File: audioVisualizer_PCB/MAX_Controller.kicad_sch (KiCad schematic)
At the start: 16 parts, among them J10 Conn_01x08_Socket, J11 Conn_01x08_Socket, J12 Conn_01x08_Socket, J5 Conn_01x08_Socket, J6 Conn_01x08_Socket, J7 Conn_01x08_Socket, J8 Conn_01x08_Socket, J9 Conn_01x08_Socket, U3 MAX7219, U4 MAX7219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

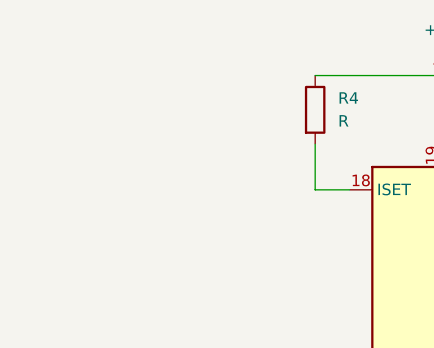
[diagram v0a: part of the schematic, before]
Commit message: migration to stm32f401
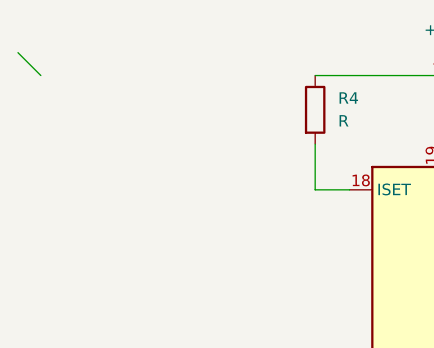
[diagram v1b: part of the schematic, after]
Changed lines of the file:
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@@
 		(color 0 0 0 0)
+	)
+	(bus_entry
+		(at 3.81 15.24)
+		(size 2.54 2.54)
+		(stroke
+			(width 0)
+			(type default)
+		)
 	)
 	(wire

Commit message: embeddeding the mcu is harder than I thought
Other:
- moved on the sheet: J5, J6, J7, J8, R4, R5, U3, U4
